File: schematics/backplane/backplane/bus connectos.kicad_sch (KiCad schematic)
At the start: 20 parts, among them J1 009159020801906, J3 PCIE-036-02-X-D-TH, J4 009159020801906, J5 PCIE-036-02-X-D-TH, J6 009159020801906, J7 PCIE-036-02-X-D-TH, J8 009159020801906, J9 PCIE-036-02-X-D-TH, Q1 BSS138, Q2 BSS138, Q3 BSS138, Q4 BSS138, Q5 BSS138, Q6 BSS138, Q7 BSS138, Q8 BSS138

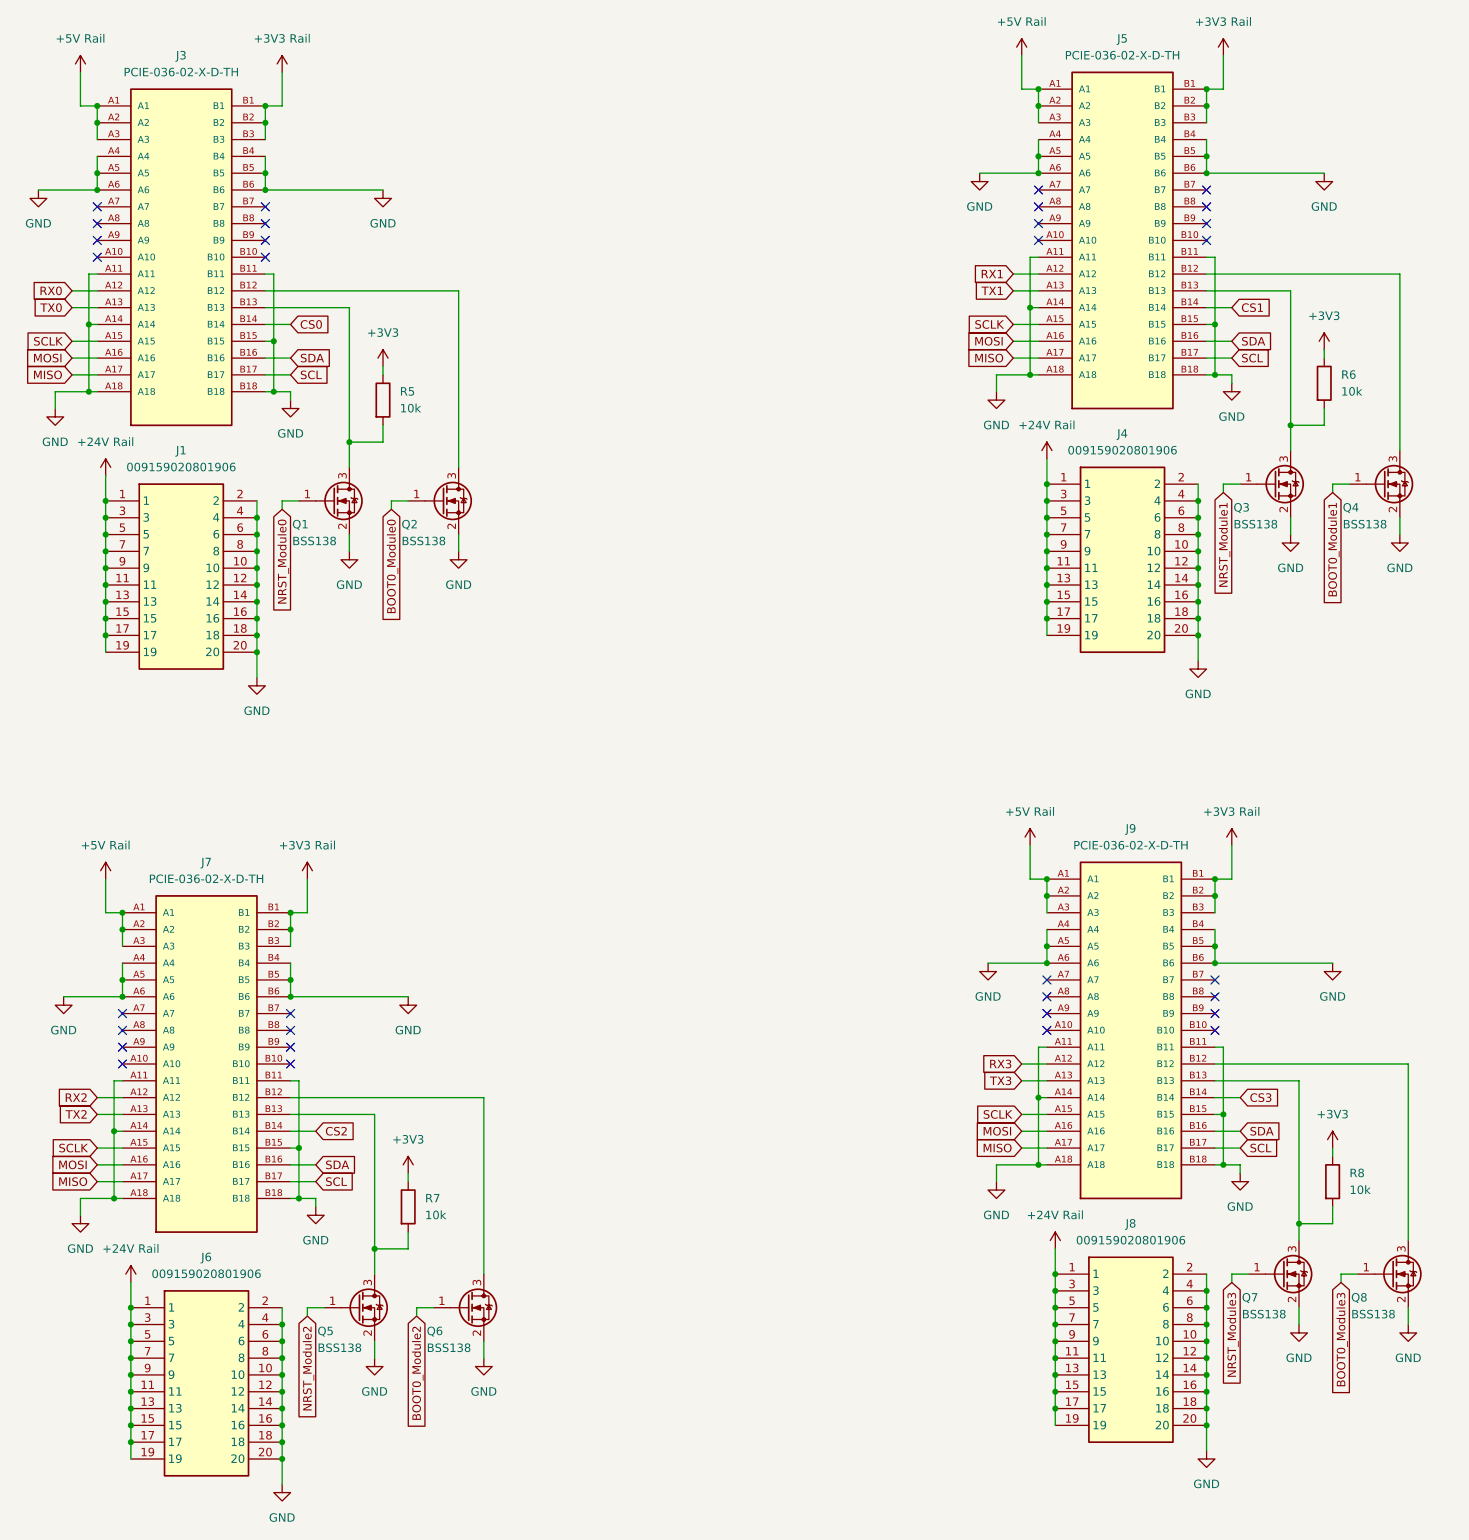
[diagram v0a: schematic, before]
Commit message: Add crystal data and Test points
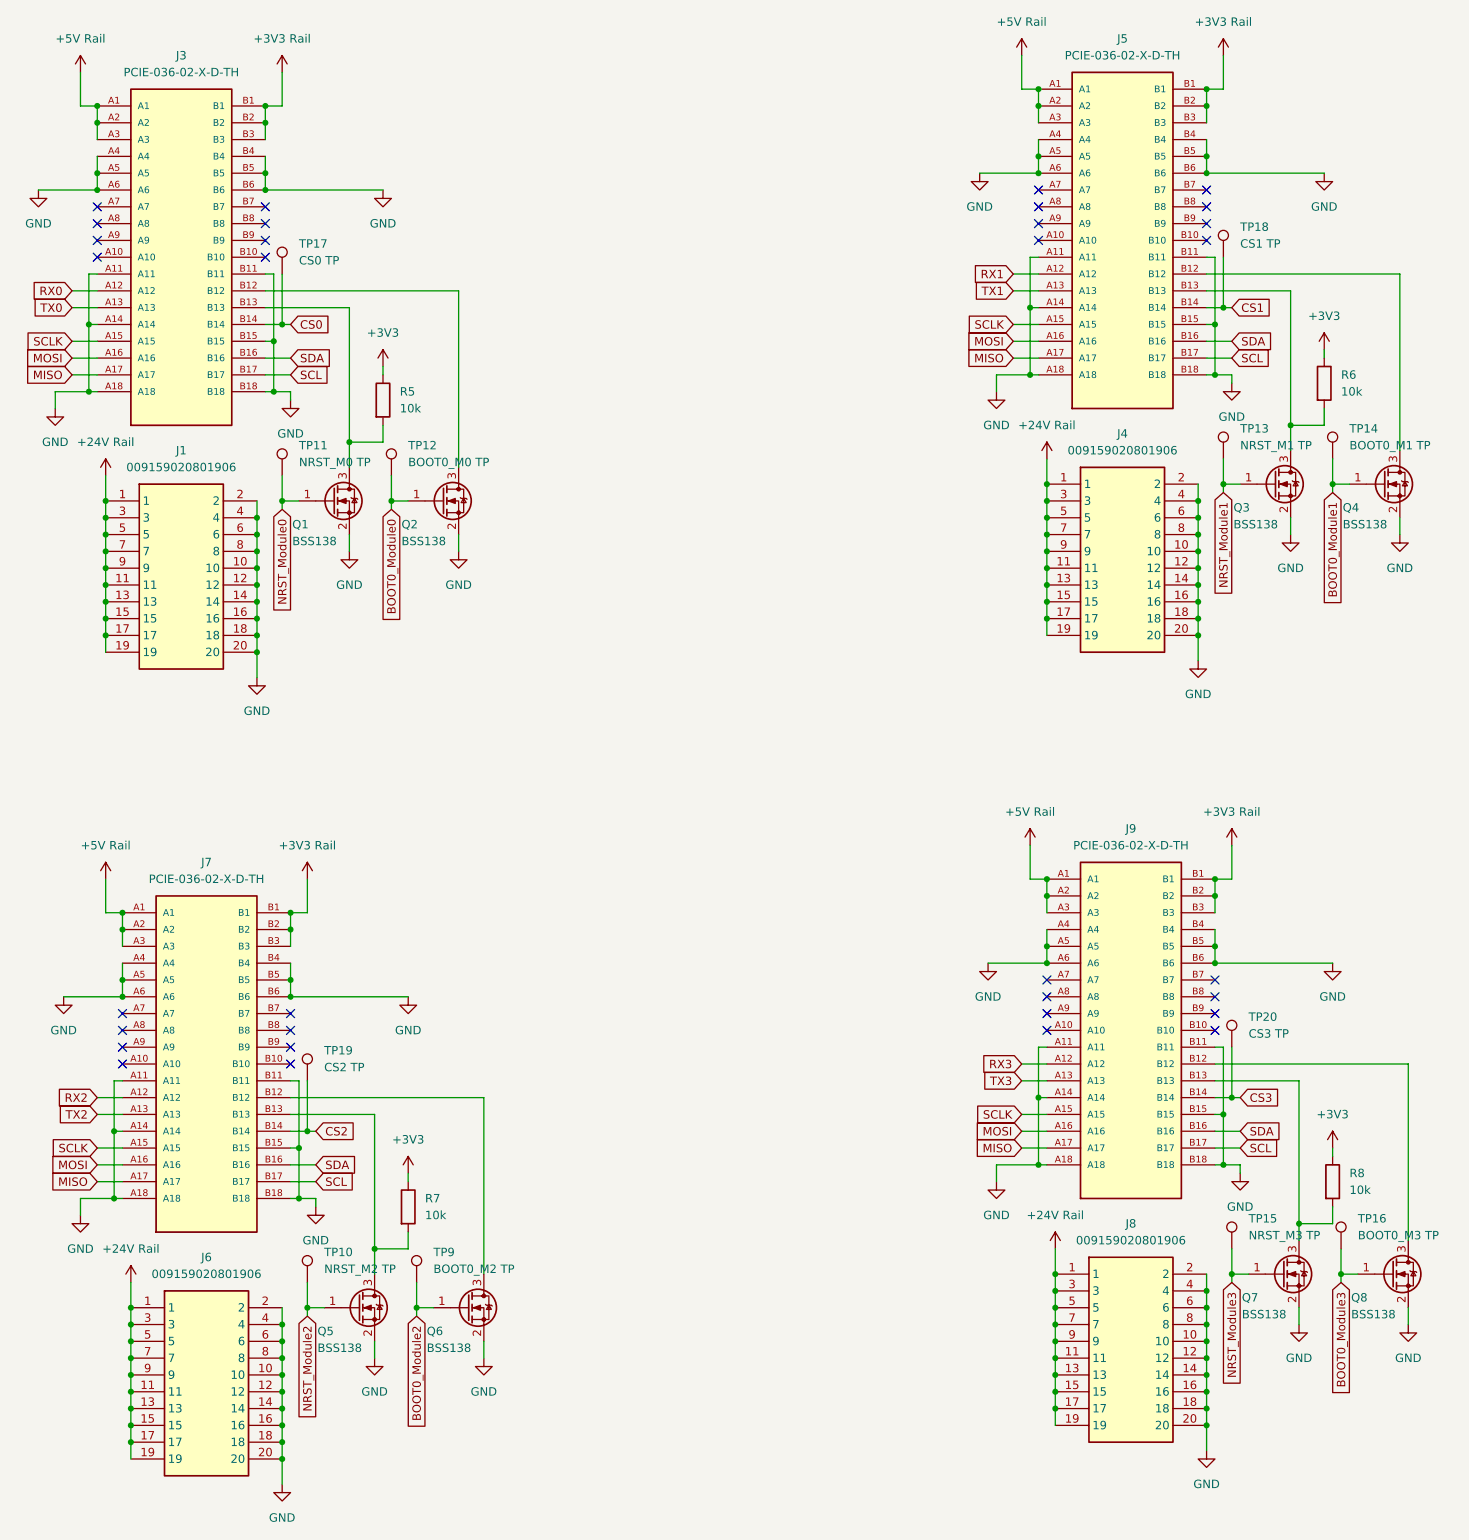
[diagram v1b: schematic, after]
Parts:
- added TP10: NRST_M2 TP, TestPoint:TestPoint_Keystone_5000-5004_Miniature, symbol Connector:TestPoint
- added TP11: NRST_M0 TP, TestPoint:TestPoint_Keystone_5000-5004_Miniature, symbol Connector:TestPoint
- added TP12: BOOT0_M0 TP, TestPoint:TestPoint_Keystone_5000-5004_Miniature, symbol Connector:TestPoint
- added TP13: NRST_M1 TP, TestPoint:TestPoint_Keystone_5000-5004_Miniature, symbol Connector:TestPoint
- added TP14: BOOT0_M1 TP, TestPoint:TestPoint_Keystone_5000-5004_Miniature, symbol Connector:TestPoint
- added TP15: NRST_M3 TP, TestPoint:TestPoint_Keystone_5000-5004_Miniature, symbol Connector:TestPoint
- added TP16: BOOT0_M3 TP, TestPoint:TestPoint_Keystone_5000-5004_Miniature, symbol Connector:TestPoint
- added TP17: CS0 TP, TestPoint:TestPoint_Keystone_5000-5004_Miniature, symbol Connector:TestPoint
- added TP18: CS1 TP, TestPoint:TestPoint_Keystone_5000-5004_Miniature, symbol Connector:TestPoint
- added TP19: CS2 TP, TestPoint:TestPoint_Keystone_5000-5004_Miniature, symbol Connector:TestPoint
- added TP20: CS3 TP, TestPoint:TestPoint_Keystone_5000-5004_Miniature, symbol Connector:TestPoint
- added TP9: BOOT0_M2 TP, TestPoint:TestPoint_Keystone_5000-5004_Miniature, symbol Connector:TestPoint
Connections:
- net BOOT0_Module0: now also TP12.1
- net BOOT0_Module1: now also TP14.1
- net BOOT0_Module2: now also TP9.1
- net BOOT0_Module3: now also TP16.1
- net CS0: now also TP17.1
- net CS1: now also TP18.1
- net CS2: now also TP19.1
- net CS3: now also TP20.1
- net NRST_Module0: now also TP11.1
- net NRST_Module1: now also TP13.1
- net NRST_Module2: now also TP10.1
- net NRST_Module3: now also TP15.1

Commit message: redo numbering
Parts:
- renumbered J9 to J10, J8 to J11, J3 to J4, J1 to J5, J5 to J6, J4 to J7, J7 to J8, J6 to J9, Q4 to Q10, Q5 to Q11, Q6 to Q12, Q7 to Q13, Q8 to Q14, Q1 to Q7, Q2 to Q8, Q3 to Q9, R5 to R21, R6 to R22, R7 to R23, R8 to R24, TP17 to TP11, TP11 to TP12, TP12 to TP13, TP18 to TP14, TP13 to TP15, TP14 to TP16, TP19 to TP17, TP10 to TP18, TP9 to TP19, TP15 to TP21, TP16 to TP22
